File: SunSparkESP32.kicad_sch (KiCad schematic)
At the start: 46 parts, among them J1 Conn_01x02_Pin, J2 USB_C_Receptacle_USB2.0, J3 Conn_01x03_Pin, J4 Conn_01x15_Pin, J5 Conn_01x03_Pin, J6 Conn_01x15_Pin, Q1 IRLML6244TRPBF, SW1 SW_Push, SW2 SW_Push, U1 ADP5090ACP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

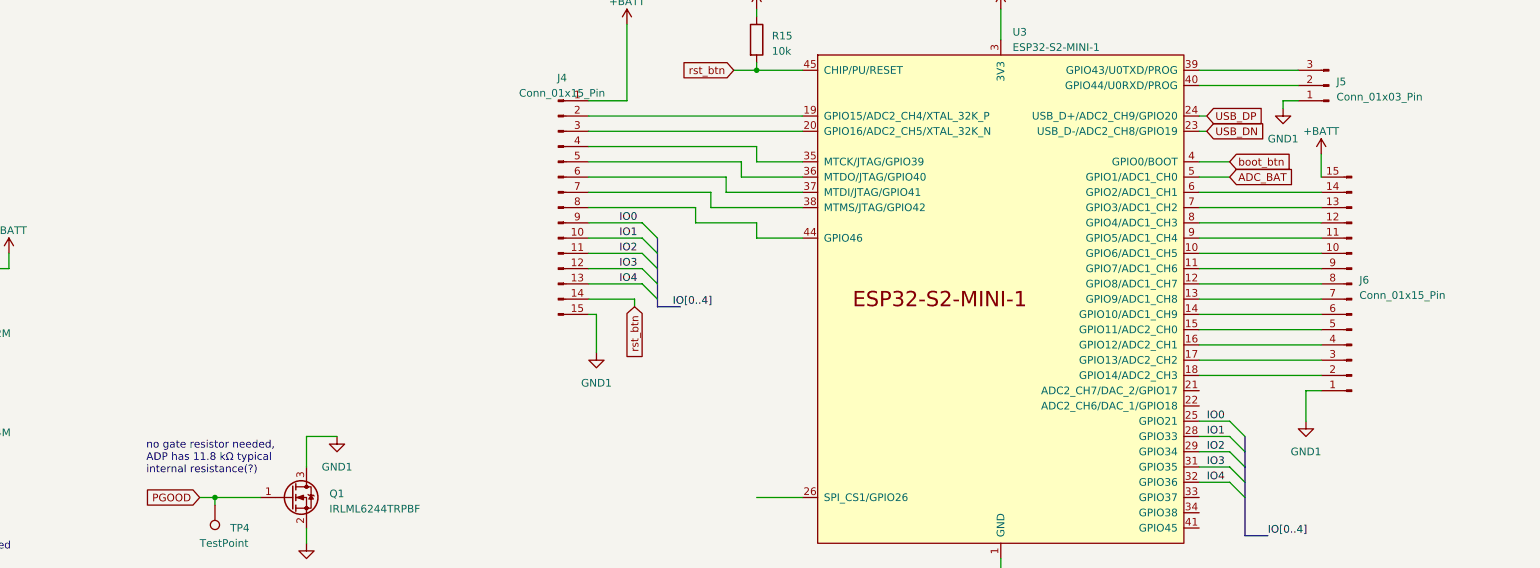
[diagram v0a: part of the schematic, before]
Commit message: Reworked placement of components Added low side switch instead of complicated high side IC Enhanced readme
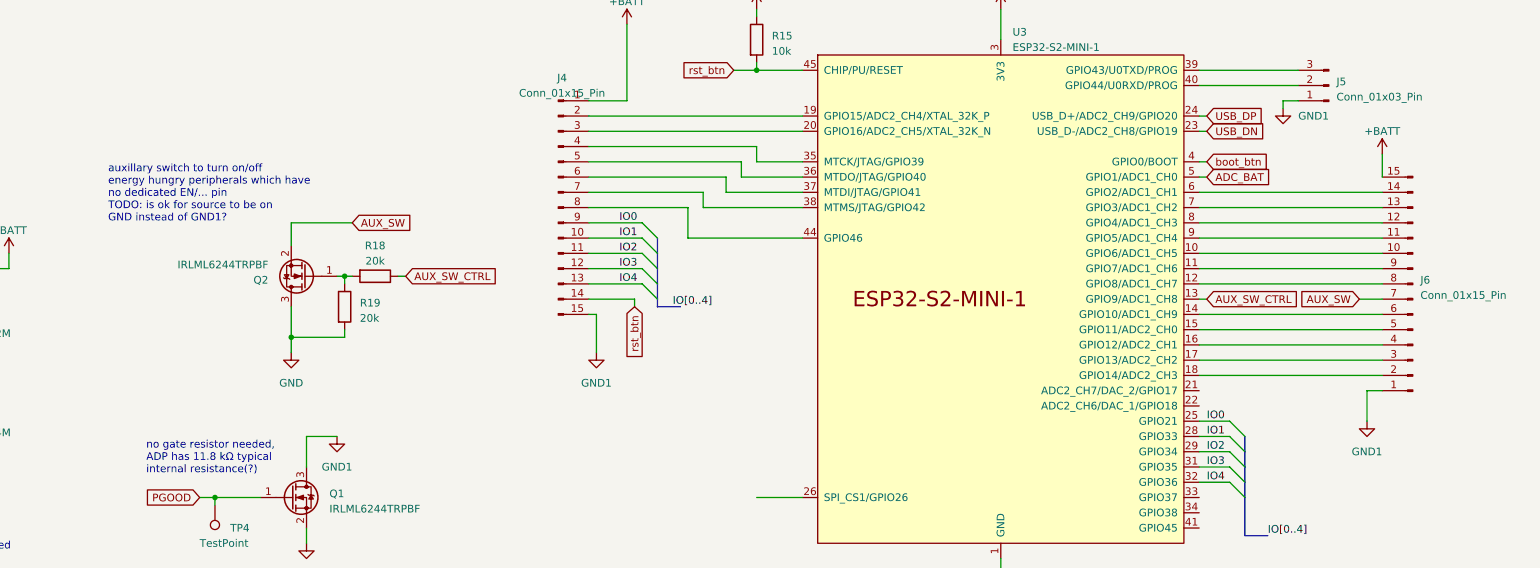
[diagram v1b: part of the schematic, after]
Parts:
- added Q2: IRLML6244TRPBF, Package_TO_SOT_SMD:SOT-23, symbol custom_sym:IRLML6244TRPBF
- added R18, R19: 20k, Resistor_SMD:R_0805_2012Metric_Pad1.20x1.40mm_HandSolder, symbol Device:R
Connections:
- net GND: now also Q2.3 (D), R19.2
- net AUX_SW: now reaches J6.7 (Pin_7)
- net AUX_SW: now also Q2.2 (S); no longer U3.13 (GPIO9/ADC1_CH8)
- new net: Q2.1 (G), R18.2, R19.1
- new net AUX_SW_CTRL: R18.1, U3.13 (GPIO9/ADC1_CH8)
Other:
- note added: "auxillary switch to turn on/off energy hungry peripherals which have no dedicated EN/... pin TODO: is ok for source to be on GND instead of GND1?"
- moved on the sheet: J6

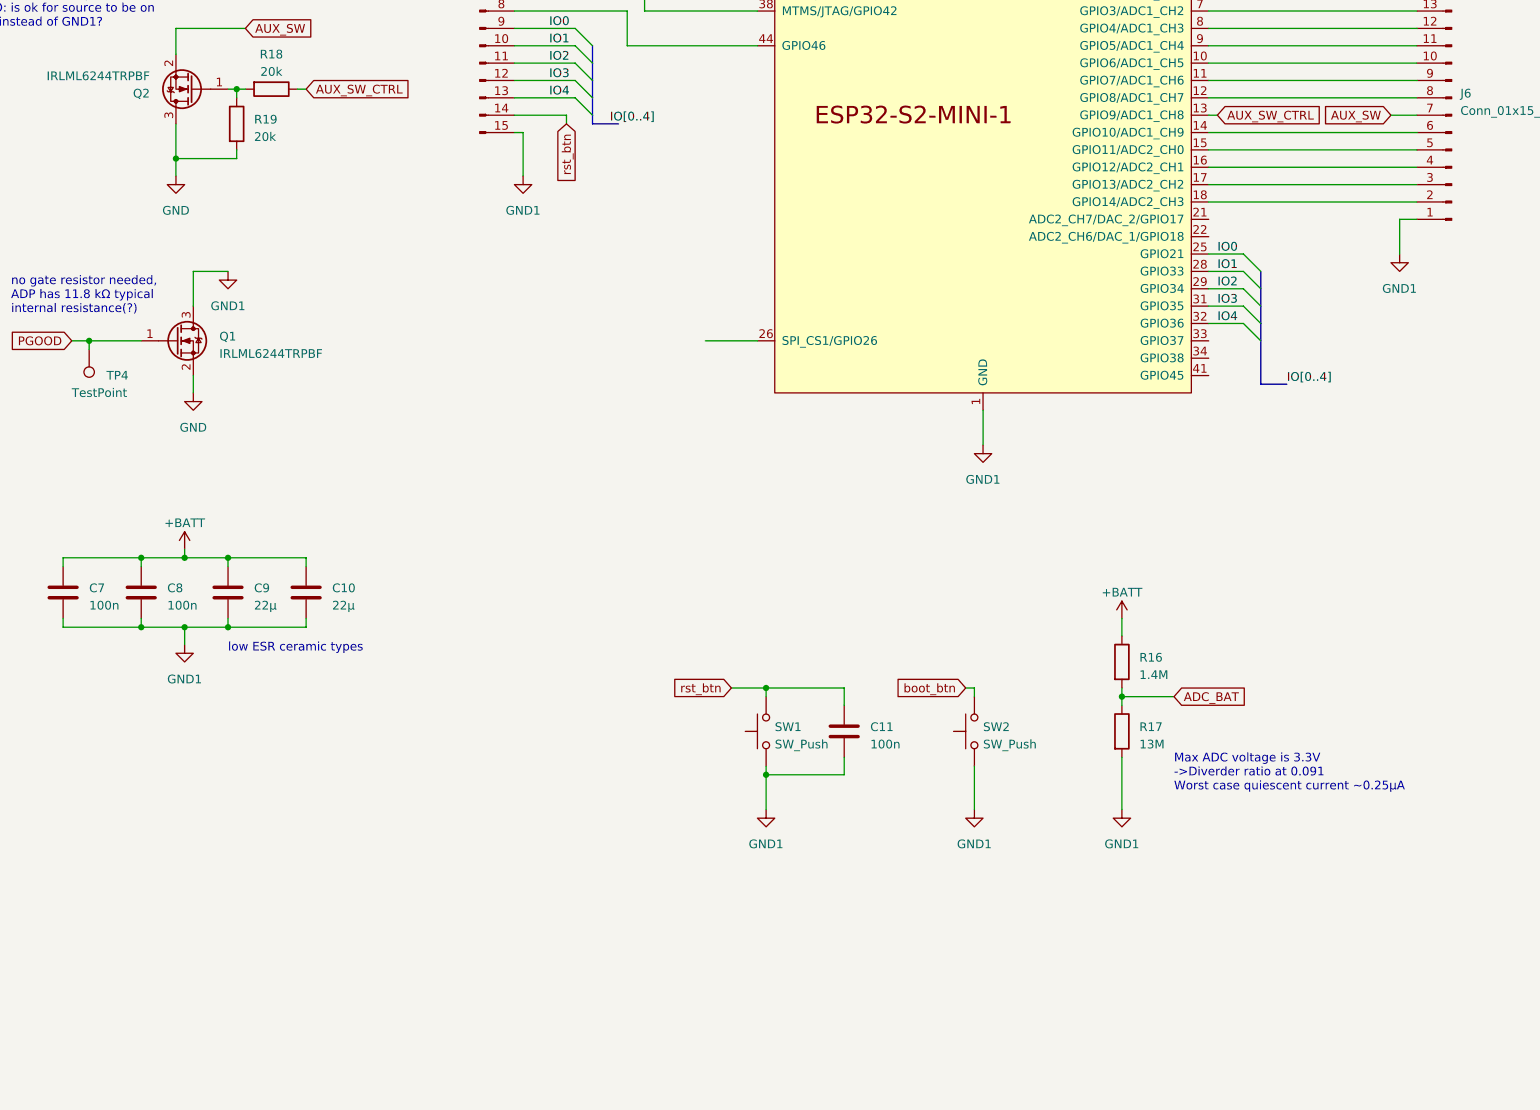
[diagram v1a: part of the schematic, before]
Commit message: Added optional footprint for RF95/96/97/98 footprint
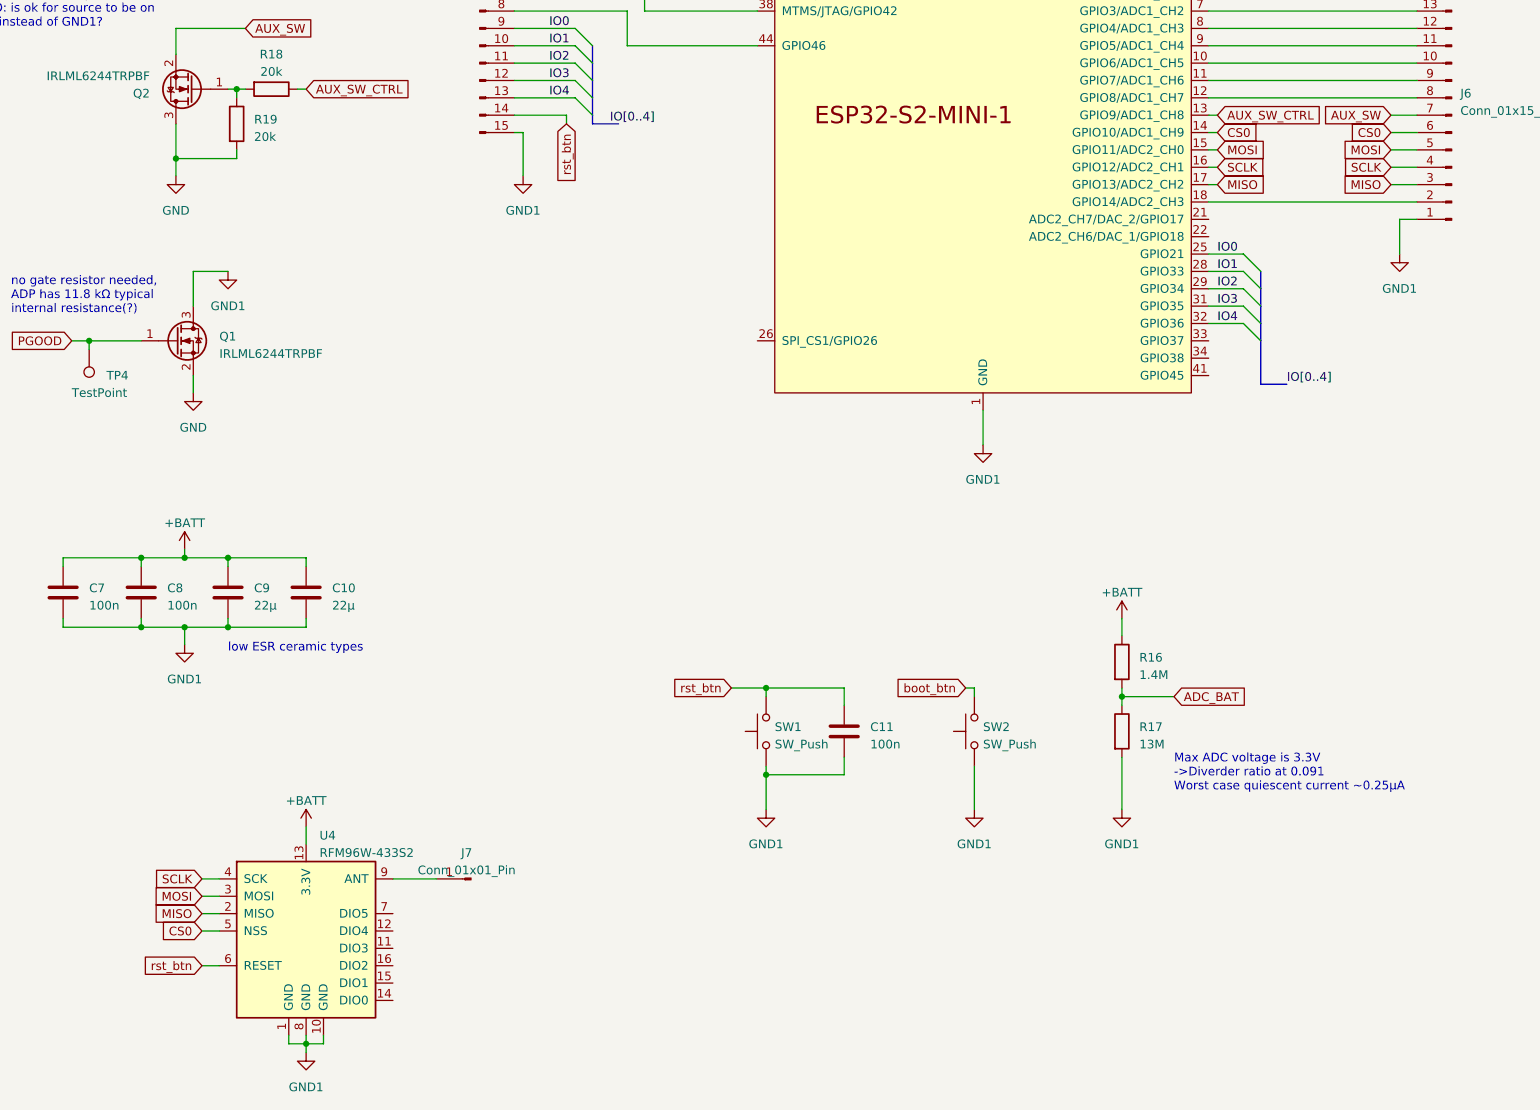
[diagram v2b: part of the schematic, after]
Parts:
- added J7: Conn_01x01_Pin, TestPoint:TestPoint_THTPad_D1.5mm_Drill0.7mm, symbol Connector:Conn_01x01_Pin
- added U4: RFM96W-433S2, RF_Module:HOPERF_RFM9XW_SMD, symbol RF_Module:RFM96W-433S2
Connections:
- net +BATT: now also U4.13 (3.3V)
- net GND1: now also U4.1 (GND), U4.10 (GND), U4.8 (GND)
- net rst_btn: now also U4.6 (RESET)
- net CS0: now reaches J6.6 (Pin_6), U3.14 (GPIO10/ADC1_CH9)
- net CS0: now also U4.5 (NSS)
- net MOSI: now reaches J6.5 (Pin_5), U3.15 (GPIO11/ADC2_CH0)
- net MOSI: now also U4.3 (MOSI)
- net SCLK: now reaches J6.4 (Pin_4), U3.16 (GPIO12/ADC2_CH1)
- net SCLK: now also U4.4 (SCK)
- net MISO: now reaches J6.3 (Pin_3), U3.17 (GPIO13/ADC2_CH2)
- net MISO: now also U4.2 (MISO)
- new net: J7.1 (Pin_1), U4.9 (ANT)
